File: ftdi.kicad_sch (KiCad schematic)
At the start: 35 parts, among them J1 USB4105-GF-A, U3 93AA56BT-I/OT, U4 FT2232HL, X1 ECS-2520MVLC-120-CN-TR

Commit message: edit README.md
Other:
- note added: "USB-C Receptacle"
- company: (none) -> NOIRLab
- title: (none) -> 4 channel ADC Module
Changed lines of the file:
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@@
 	(generator_version "9.0")
 	(paper "A4")
+	(title_block
+		(title "4 channel ADC Module")
+		(date "2025-04-18")
+		(rev "0.1")
+		(company "NOIRLab")
+		(comment 1 "Design: Braulio Cancino Vera - braulio.cancino@noirlab.edu")
+	)
+	(text "USB-C Receptacle"
+		(exclude_from_sim no)
+		(at 39.116 126.238 0)
+		(effects
+			(font
+				(size 1.27 1.27)
+			)
+		)
+	)
 	(junction
 		(at 199.39 30.48)

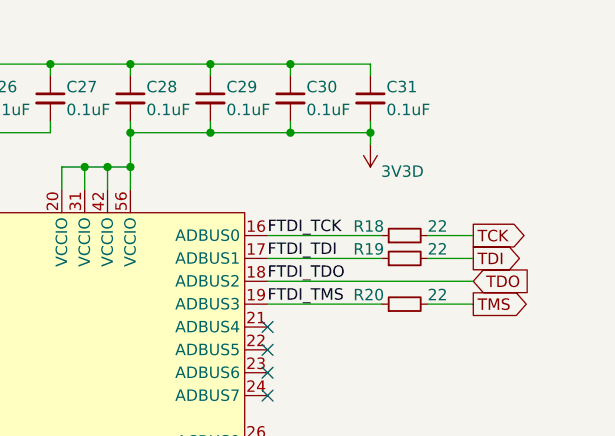
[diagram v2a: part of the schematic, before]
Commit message: Added clock sync and fix minor errors.
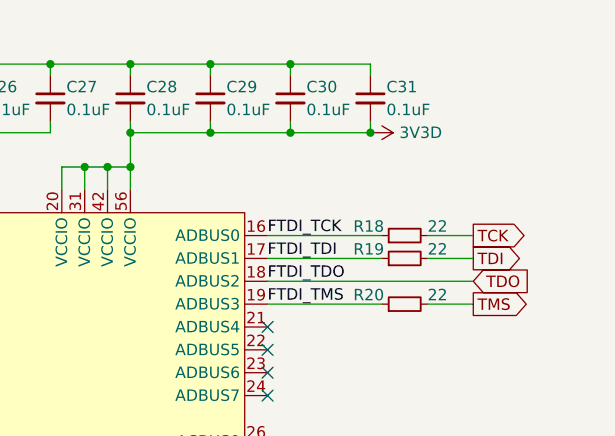
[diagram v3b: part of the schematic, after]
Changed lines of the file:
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@@
 	(title_block
 		(title "4 channel ADC Module")
-		(date "2025-04-18")
+		(date "2025-05-06")
 		(rev "0.1")
 		(company "NOIRLab")
@@
 	(wire
 		(pts
-			(xy 234.95 39.37) (xy 234.95 38.1)
-		)
-		(stroke
-			(width 0)
-			(type default)
-		)
-	)
-	(wire
-		(pts
 			(xy 35.56 158.75) (xy 53.34 158.75)
 		)
@@
 	(symbol
 		(lib_id "power:+3V3")
-		(at 234.95 39.37 0)
+		(at 234.95 38.1 270)
 		(mirror x)
 		(unit 1)
@@
 		(dnp no)
 		(property "Reference" "#PWR035"
-			(at 234.95 35.56 0)
+			(at 231.14 38.1 0)
 			(effects
 				(font
@@
 		)
 		(property "Value" "3V3D"
-			(at 238.506 42.418 0)
+			(at 240.538 38.1 90)
 			(effects
 				(font
@@
 		)
 		(property "Footprint" ""
-			(at 234.95 39.37 0)
+			(at 234.95 38.1 0)
 			(effects
 				(font
@@
 		)
 		(property "Datasheet" ""
-			(at 234.95 39.37 0)
+			(at 234.95 38.1 0)
 			(effects
 				(font
@@
 		)
 		(property "Description" "Power symbol creates a global label with name \"+3V3\""
-			(at 234.95 39.37 0)
+			(at 234.95 38.1 0)
 			(effects
 				(font
